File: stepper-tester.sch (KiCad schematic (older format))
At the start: 14 parts, among them J1 Barrel_Jack, J2 Conn_01x04_Male, SW1 SW_Push_DPDT, SW2 SW_Push_DPDT, U1 NE555P, U2 AMS1117-5.0

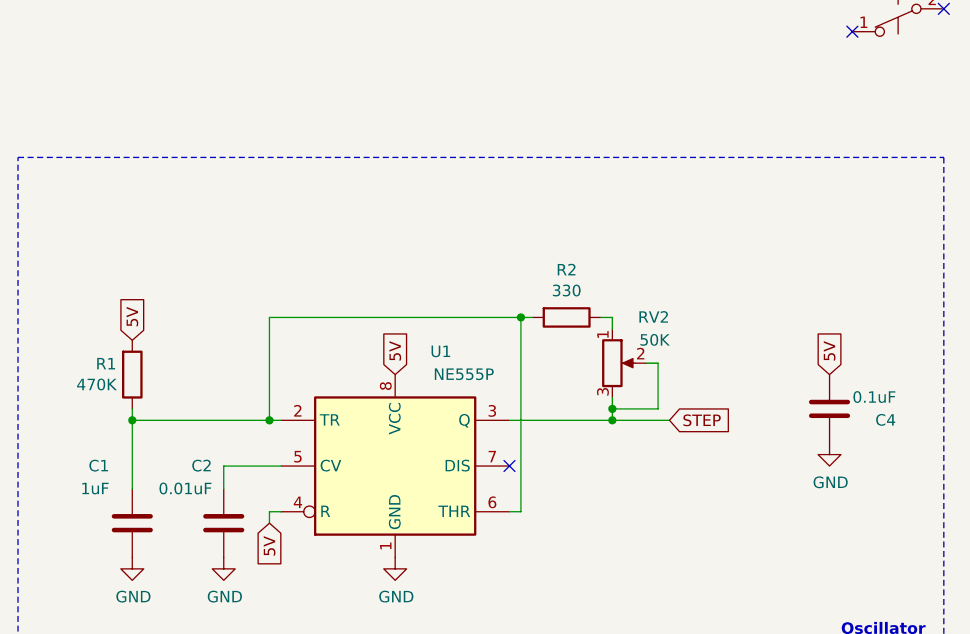
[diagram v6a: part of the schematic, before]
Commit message: 50% duty cycle 555 schematics
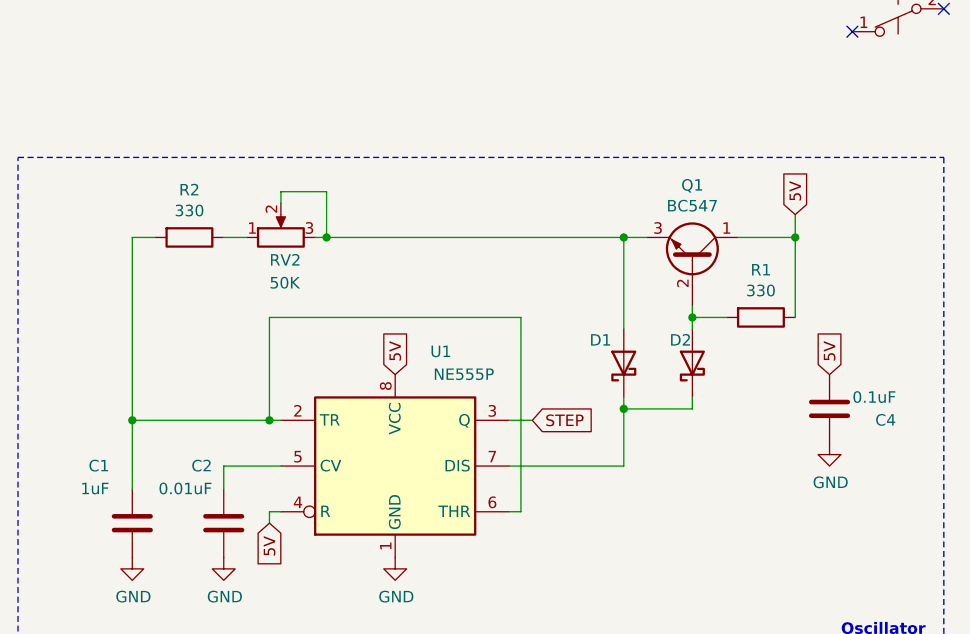
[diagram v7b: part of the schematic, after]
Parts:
- added D1, D2: 1N5817, Diode_THT:D_DO-41_SOD81_P10.16mm_Horizontal, symbol Diode:1N5817
- added Q1: BC547, Package_TO_SOT_THT:TO-92_Inline, symbol Transistor_BJT:BC547
- R1: value 470K -> 330
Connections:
- net 5V: now also R1.1, Q1.1 (C); no longer R1.2
- net STEP: no longer RV2.2, RV2.3
- net at C1.2, R2.2, U1.2 (TR)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: no longer R1.1
- net at U1.7 (DIS): now also D1.1 (K), D2.1 (K)
- new net: D1.2 (A), Q1.3 (E), RV2.2, RV2.3
- new net: D2.2 (A), Q1.2 (B), R1.2
- no-connect marks 11 -> 10
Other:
- moved on the sheet: R2, RV2
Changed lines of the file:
@@
 L Device:R_POT RV2
 U 1 1 5F1FB82A
-P 3600 5000
-F 0 "RV2" H 3850 5200 50  0000 R CNN
-F 1 "50K" H 3850 5100 50  0000 R CNN
-F 2 "Connector_PinHeader_2.54mm:PinHeader_1x03_P2.54mm_Vertical" H 3600 5000 50  0001 C CNN
-F 3 "~" H 3600 5000 50  0001 C CNN
-	1    3600 5000
-	1    0    0    -1
-$EndComp
-$Comp
-L Device:R R1
-U 1 1 5F1FDF15
-P 1500 5050
-F 0 "R1" H 1431 5004 50  0000 R CNN
-F 1 "470K" H 1431 5095 50  0000 R CNN
-F 2 "Resistor_THT:R_Axial_DIN0207_L6.3mm_D2.5mm_P2.54mm_Vertical" V 1430 5050 50  0001 C CNN
-F 3 "~" H 1500 5050 50  0001 C CNN
-	1    1500 5050
-	1    0    0    1
-$EndComp
-Wire Wire Line
-	3150 5250 3600 5250
+P 2150 4450
+F 0 "RV2" V 2050 4500 50  0000 R CNN
+F 1 "50K" V 1950 4500 50  0000 R CNN
+F 2 "Connector_PinHeader_2.54mm:PinHeader_1x03_P2.54mm_Vertical" H 2150 4450 50  0001 C CNN
+F 3 "~" H 2150 4450 50  0001 C CNN
+	1    2150 4450
+	0    -1   -1   0
+$EndComp
 Text GLabel 7050 2350 0    50   Input ~ 0
 STEP
-Connection ~ 3600 5250
-Wire Wire Line
-	3600 5250 3850 5250
 Wire Wire Line
 	2100 5250 2150 5250
 Wire Wire Line
-	3750 5000 3800 5000
-Wire Wire Line
-	3600 5150 3600 5200
-Text GLabel 1500 4900 1    50   Input ~ 0
-5V
-Wire Wire Line
 	2100 5700 2100 5650
 Wire Wire Line
 	2100 5650 2150 5650
-Wire Wire Line
-	3600 4850 3600 4800
-Wire Wire Line
-	3800 5000 3800 5200
-Wire Wire Line
-	3800 5200 3600 5200
-Connection ~ 3600 5200
-Wire Wire Line
-	3600 5200 3600 5250
-NoConn ~ 3150 5450
 $Comp
 L power:GND #PWR0106
@@
 	1    0    0    -1
 $EndComp
-Wire Wire Line
-	1500 5200 1500 5250
 Wire Wire Line
 	2100 5250 1500 5250
@@
 Text Notes 4600 6200 0    50   ~ 10
 Oscillator
-Text GLabel 3850 5250 2    50   Input ~ 0
-STEP
 Wire Wire Line
 	2100 4800 2100 5250
 Wire Wire Line
 	3200 4800 2100 4800
-Connection ~ 3200 4800
 Wire Wire Line
 	3200 5650 3200 4800
-Wire Wire Line
-	3250 4800 3200 4800
-Wire Wire Line
-	3600 4800 3550 4800
 $Comp
 L Device:R R2
 U 1 1 5F1FC01A
-P 3400 4800
-F 0 "R2" V 3193 4800 50  0000 C CNN
-F 1 "330" V 3284 4800 50  0000 C CNN
-F 2 "Resistor_THT:R_Axial_DIN0207_L6.3mm_D2.5mm_P2.54mm_Vertical" V 3330 4800 50  0001 C CNN
-F 3 "~" H 3400 4800 50  0001 C CNN
-	1    3400 4800
+P 1750 4450
+F 0 "R2" V 1543 4450 50  0000 C CNN
+F 1 "330" V 1634 4450 50  0000 C CNN
+F 2 "Resistor_THT:R_Axial_DIN0207_L6.3mm_D2.5mm_P2.54mm_Vertical" V 1680 4450 50  0001 C CNN
+F 3 "~" H 1750 4450 50  0001 C CNN
+	1    1750 4450
 	0    1    1    0
 $EndComp
@@
 	4500 3150 4650 3150
 $Comp
-L Timer:NE555P U1
-U 1 1 5F2154E9
-P 2650 5450
-F 0 "U1" H 2850 5950 50  0000 C CNN
-F 1 "NE555P" H 2950 5850 50  0000 C CNN
-F 2 "Package_SO:SO-8_5.3x6.2mm_P1.27mm" H 3300 5050 50  0001 C CNN
-F 3 "http://www.ti.com/lit/ds/symlink/ne555.pdf" H 3500 5050 50  0001 C CNN
-	1    2650 5450
-	1    0    0    -1
-$EndComp
-$Comp
 L Regulator_Linear:AMS1117-5.0 U2
 U 1 1 5F228A3F
@@
 Wire Wire Line
 	2000 1350 2600 1350
+$Comp
+L Diode:1N5817 D1
+U 1 1 5F7C5908
+P 3650 5000
+F 0 "D1" V 3750 5150 50  0000 R CNN
+F 1 "1N5817" V 3750 5300 50  0001 R CNN
+F 2 "Diode_THT:D_DO-41_SOD81_P10.16mm_Horizontal" H 3650 4825 50  0001 C CNN
+F 3 "http://www.vishay.com/docs/88525/1n5817.pdf" H 3650 5000 50  0001 C CNN
+	1    3650 5000
+	0    -1   -1   0
+$EndComp
+Wire Wire Line
+	3150 5250 3250 5250
+$Comp
+L Device:R R1
+U 1 1 5F7CF699
+P 4250 4800
+F 0 "R1" V 4043 4800 50  0000 C CNN
+F 1 "330" V 4134 4800 50  0000 C CNN
+F 2 "Resistor_THT:R_Axial_DIN0207_L6.3mm_D2.5mm_P2.54mm_Vertical" V 4180 4800 50  0001 C CNN
+F 3 "~" H 4250 4800 50  0001 C CNN
+	1    4250 4800
+	0    1    1    0
+$EndComp
+$Comp
+L Diode:1N5817 D2
+U 1 1 5F7D258F
+P 3950 5000
+F 0 "D2" V 4050 5100 50  0000 R CNN
+F 1 "1N5817" V 3905 4920 50  0001 R CNN
+F 2 "Diode_THT:D_DO-41_SOD81_P10.16mm_Horizontal" H 3950 4825 50  0001 C CNN
+F 3 "http://www.vishay.com/docs/88525/1n5817.pdf" H 3950 5000 50  0001 C CNN
+	1    3950 5000
+	0    -1   -1   0
+$EndComp
+Wire Wire Line
+	3650 4850 3650 4450
+Wire Wire Line
+	3650 5200 3650 5450
+Wire Wire Line
+	3650 5450 3150 5450
+$Comp
+L Timer:NE555P U1
+U 1 1 5F2154E9
+P 2650 5450
+F 0 "U1" H 2850 5950 50  0000 C CNN
+F 1 "NE555P" H 2950 5850 50  0000 C CNN
+F 2 "Package_SO:SO-8_5.3x6.2mm_P1.27mm" H 3300 5050 50  0001 C CNN
+F 3 "http://www.ti.com/lit/ds/symlink/ne555.pdf" H 3500 5050 50  0001 C CNN
+	1    2650 5450
+	1    0    0    -1
+$EndComp
+Text GLabel 3250 5250 2    50   Input ~ 0
+STEP
+Wire Wire Line
+	2150 4300 2150 4250
+Wire Wire Line
+	2150 4250 2350 4250
+Wire Wire Line
+	2350 4250 2350 4450
+Wire Wire Line
+	2350 4450 3650 4450
+Connection ~ 3650 4450
+Wire Wire Line
+	2350 4450 2300 4450
+Connection ~ 2350 4450
+Wire Wire Line
+	2000 4450 1900 4450
+Wire Wire Line
+	1600 4450 1500 4450
+Wire Wire Line
+	3650 4450 3750 4450
+Wire Wire Line
+	3950 4750 3950 4800
+$Comp
+L Transistor_BJT:BC547 Q1
+U 1 1 5F7CA031
+P 3950 4550
+F 0 "Q1" V 4278 4550 50  0000 C CNN
+F 1 "BC547" V 4187 4550 50  0000 C CNN
+F 2 "Package_TO_SOT_THT:TO-92_Inline" H 4150 4475 50  0001 L CIN
+F 3 "http://www.fairchildsemi.com/ds/BC/BC547.pdf" H 3950 4550 50  0001 L CNN
+	1    3950 4550
+	0    1    -1   0
+$EndComp
+Wire Wire Line
+	3650 5200 3950 5200
+Wire Wire Line
+	3950 5200 3950 5150
+Wire Wire Line
+	3650 5200 3650 5150
+Connection ~ 3650 5200
+Text GLabel 4400 4350 1    50   Input ~ 0
+5V
+Wire Wire Line
+	4400 4350 4400 4450
+Wire Wire Line
+	4150 4450 4400 4450
+Connection ~ 4400 4450
+Wire Wire Line
+	4400 4450 4400 4800
+Wire Wire Line
+	4100 4800 3950 4800
+Connection ~ 3950 4800
+Wire Wire Line
+	3950 4800 3950 4850
+Wire Wire Line
+	1500 4450 1500 5250
 $EndSCHEMATC

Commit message: PCB WIP
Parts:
- Q1: footprint Package_TO_SOT_THT:TO-92_Inline -> Package_TO_SOT_THT:TO-92L_Inline_Wide
- R1: value 330 -> 1K
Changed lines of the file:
@@
 P 4250 4800
 F 0 "R1" V 4043 4800 50  0000 C CNN
-F 1 "330" V 4134 4800 50  0000 C CNN
+F 1 "1K" V 4134 4800 50  0000 C CNN
 F 2 "Resistor_THT:R_Axial_DIN0207_L6.3mm_D2.5mm_P2.54mm_Vertical" V 4180 4800 50  0001 C CNN
 F 3 "~" H 4250 4800 50  0001 C CNN
@@
 F 0 "Q1" V 4278 4550 50  0000 C CNN
 F 1 "BC547" V 4187 4550 50  0000 C CNN
-F 2 "Package_TO_SOT_THT:TO-92_Inline" H 4150 4475 50  0001 L CIN
+F 2 "Package_TO_SOT_THT:TO-92L_Inline_Wide" H 4150 4475 50  0001 L CIN
 F 3 "http://www.fairchildsemi.com/ds/BC/BC547.pdf" H 3950 4550 50  0001 L CNN
 	1    3950 4550
